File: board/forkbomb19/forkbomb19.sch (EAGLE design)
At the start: 85 parts, among them T3 MMUN2133LT1G, U1 ESP-WROOM-03, U4 TPS61090RSAR, U5 MCP73871

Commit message: working on rev 1.1
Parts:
- removed B1: JST 2-PH, microbuilder:BATTERY
- removed C10: 100uF, rcl:CPOL-USC/6032-28R
- removed C15: 2.2uF, rcl:C-USC0805
- removed C16: 100nF, rcl:C-USC0603
- removed CHRG: ORANGE, led:LEDCHIP-LED0603
- removed DONE: GREEN, led:LEDCHIP-LED0603
- removed R25: 270K, rcl:R-US_R0603
- removed R26, R30: 100K, rcl:R-US_R0603
- removed R27, R28: 1K, rcl:R-US_R0603
- removed R29: 1.0K, rcl:R-US_R0603
- removed THERM: 15K, rcl:R-US_R0603
- removed TP_BATT_VLIPO: TPSTP20SQ, testpad:TPSTP20SQ
- removed U5: MCP73871, microbuilder:MCP73871
- added C4: 100uF, resistor:CPOL-USC/6032-28R
- added C5: 100nF, rcl:C-USC0603
- added R14: (no value), rcl:R-US_R1210
- added VBAT_GND, VBAT_V: POT_GND, con-samtec:TSW-101-07-G-S
- R24: value 1.87M -> 1.33M
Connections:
- removed net N$28: R25.1, R26.1, U5.VPCC
- removed net N$29: R28.1, U5.STAT2
- removed net N$32: R27.1, U5.STAT1/LBO
- removed net N$33: R29.2, U5.PROG1
- removed net N$34: THERM.2, U5.THERM
- removed net N$35: DONE.C, R28.2
- removed net N$36: CHRG.C, R27.2
- removed net N$37: R30.2, U5.PROG3
- removed net N$42: R18.2, U$8.P$1, U$8.P$4
- removed net VLIPO: B1.+, C10.+, TP_BATT_VLIPO.PP, U5.VBAT1, U5.VBAT2, U5.VBATSENS
- new net N$15: R7.1, T2.B
- new net N$17: R6.1, T1.B
- net +3V3: now also C4.+, C5.1, R14.2; no longer C15.1, U$2.LED_VCC
- net DAT_TERM_RDY: now also T1.E
- net GND: now also C4.-, C5.2, VBAT_GND.1; no longer B1.-, C10.-, C15.2, C16.2, R26.2, R29.1, R30.1, THERM.1, U5.THERMAL, U5.VSS1, U5.VSS2
- net N$1: now also R14.1, U$2.LED_VCC; no longer R7.1, T1.E, T2.B
- net N$13: now also U$8.P$1, U$8.P$4; no longer U$8.P$3, U$8.P$6
- net N$3: now also R18.2, U$8.P$3, U$8.P$6; no longer R6.1, T1.B, T2.E
- net RDY_2_SND: now also T2.E
- net VBAT: now also VBAT_V.1; no longer C16.1, U5.VOUT1, U5.VOUT2
- net VBUS: no longer CHRG.A, DONE.A, R25.2, U5./TE, U5.CE, U5.PROG2, U5.SEL, U5.VIN1, U5.VIN2
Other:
- note added: "1.1"
- note removed: "1.0"
- moved on the sheet: C13, C14, C2, L1, LOGO_B, LOGO_G, LOGO_R, LOW_BATT, R13, R18, R19, R20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

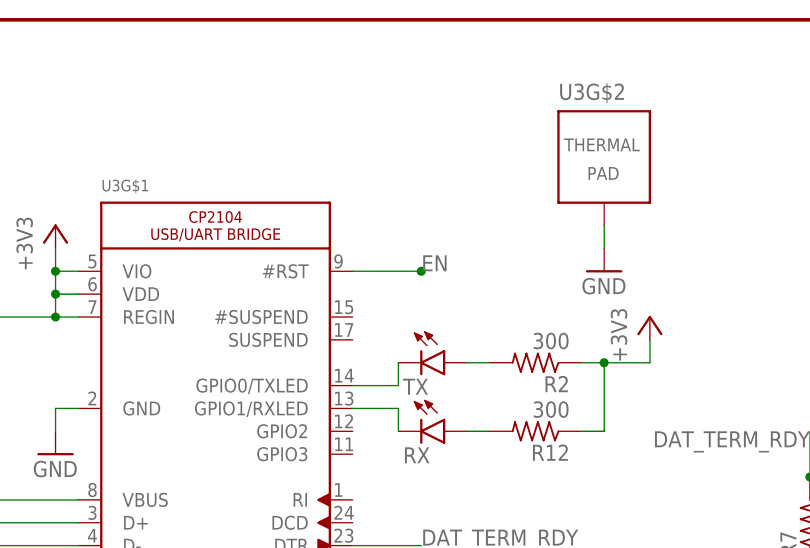
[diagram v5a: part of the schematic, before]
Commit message: started doing layout for rev 1.1
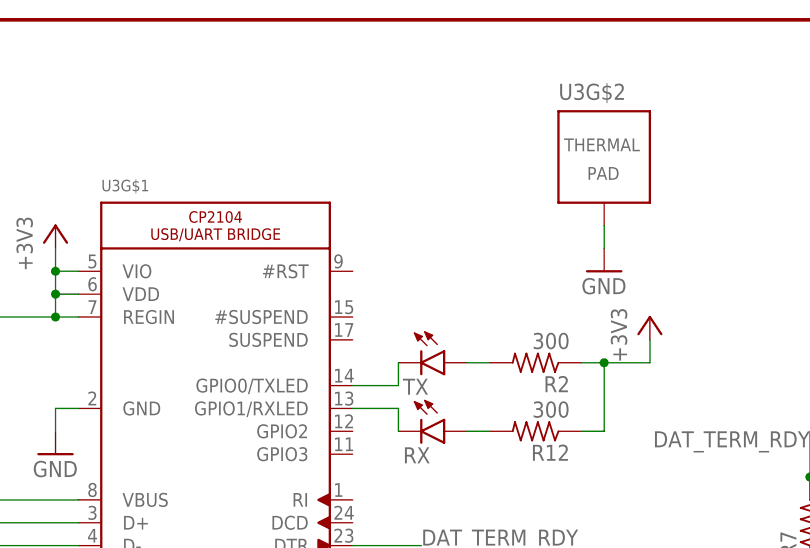
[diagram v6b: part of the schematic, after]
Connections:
- net EN: no longer U3G$1.#RST
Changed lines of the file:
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@@
 <label x="193.04" y="48.26" size="1.778" layer="95" rot="R270"/>
-</segment>
-<segment>
-<pinref part="U3" gate="G$1" pin="#RST"/>
-<wire x1="152.4" y1="91.44" x2="160.02" y2="91.44" width="0.1524" layer="91"/>
-<label x="160.02" y="91.44" size="1.778" layer="95"/>
-<junction x="160.02" y="91.44"/>
 </segment>
 </net>
